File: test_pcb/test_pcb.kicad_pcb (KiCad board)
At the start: 2 copper layers, 2 parts

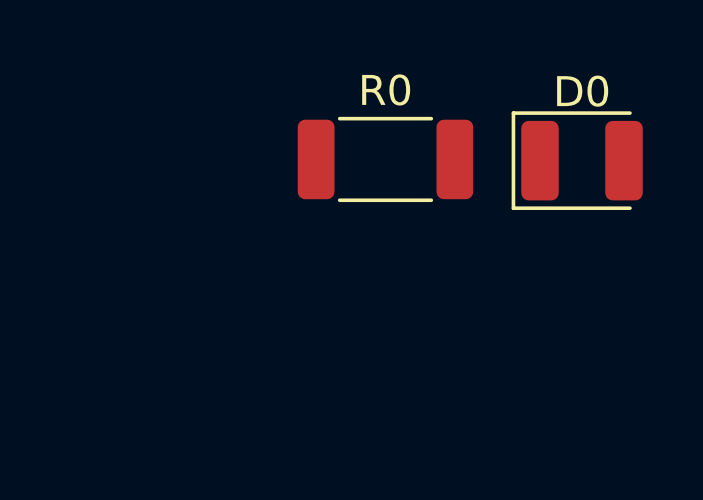
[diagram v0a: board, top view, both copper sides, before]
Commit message: added loading for segments and vias
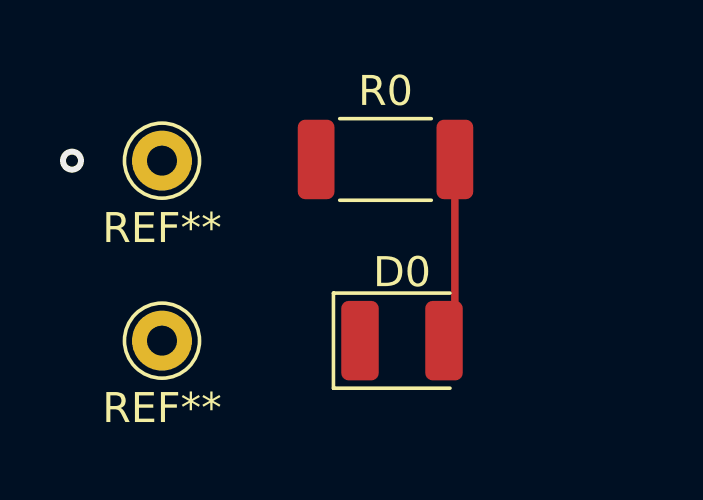
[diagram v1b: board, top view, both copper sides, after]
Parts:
- added REF**: Pin_D1.0mm_L10.0mm, Connector_Pin:Pin_D1.0mm_L10.0mm, F.Cu at (28.0, 39.0)
- added REF**: Pin_D1.0mm_L10.0mm, Connector_Pin:Pin_D1.0mm_L10.0mm, F.Cu at (28.0, 33.0)
- moved D0 8.49 mm to (36.0, 39.0)
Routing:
- net Net-(D0-Pad2): track 0.00 -> 6.19 mm
- net (no net): vias 0 -> 1
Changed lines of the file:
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@@
   (net 2 "Net-(D0-Pad2)")
   (net 3 "+5V")
+  (footprint "Connector_Pin:Pin_D1.0mm_L10.0mm" (layer "F.Cu")
+    (at 28 39)
+    (descr "solder Pin_ diameter 1.0mm, hole diameter 1.0mm (press fit), length 10.0mm")
+    (tags "solder Pin_ press fit")
+    (attr through_hole)
+    (fp_text reference "REF**" (at 0 2.25) (layer "F.SilkS")
+      (effects (font (size 1 1) (thickness 0.15)))
+    )
+    (fp_text value "Pin_D1.0mm_L10.0mm" (at 0 -2.05) (layer "F.Fab")
+      (effects (font (size 1 1) (thickness 0.15)))
+    )
+    (fp_text user "${REFERENCE}" (at 0 2.25) (layer "F.Fab")
+      (effects (font (size 1 1) (thickness 0.15)))
+    )
+    (fp_circle (center 0 0) (end 1.25 0.05) (layer "F.SilkS") (width 0.12) (fill none))
+    (fp_circle (center 0 0) (end 1.5 0) (layer "F.CrtYd") (width 0.05) (fill none))
+    (fp_circle (center 0 0) (end 0.5 0) (layer "F.Fab") (width 0.12) (fill none))
+    (fp_circle (center 0 0) (end 1 0) (layer "F.Fab") (width 0.12) (fill none))
+    (pad "1" thru_hole circle (at 0 0) (size 2 2) (drill 1) (layers *.Cu *.Mask)
+      (net 1 "GND"))
+    (model "${KICAD6_3DMODEL_DIR}/Connector_Pin.3dshapes/Pin_D1.0mm_L10.0mm.wrl"
+      (offset (xyz 0 0 0))
+      (scale (xyz 1 1 1))
+      (rotate (xyz 0 0 0))
+    )
+  )
   (footprint "LED_SMD:LED_1210_3225Metric" (layer "F.Cu")
-    (at 42 33)
+    (at 36 39)
     (descr "LED SMD 1210 (3225 Metric), square (rectangular) end terminal, IPC_7351 nominal, (Body size source: http://www.tortai-tech.com/upload/download/2011102023233369053.pdf), generated with kicad-footprint-generator")
     (tags "LED")
@@
       (net 2 "Net-(D0-Pad2)") (pinfunction "A") (pintype "passive"))
     (model "${KICAD6_3DMODEL_DIR}/LED_SMD.3dshapes/LED_1210_3225Metric.wrl"
+      (offset (xyz 0 0 0))
+      (scale (xyz 1 1 1))
+      (rotate (xyz 0 0 0))
+    )
+  )
+  (footprint "Connector_Pin:Pin_D1.0mm_L10.0mm" (layer "F.Cu")
+    (at 28 33)
+    (descr "solder Pin_ diameter 1.0mm, hole diameter 1.0mm (press fit), length 10.0mm")
+    (tags "solder Pin_ press fit")
+    (attr through_hole)
+    (fp_text reference "REF**" (at 0 2.25) (layer "F.SilkS")
+      (effects (font (size 1 1) (thickness 0.15)))
+    )
+    (fp_text value "Pin_D1.0mm_L10.0mm" (at 0 -2.05) (layer "F.Fab")
+      (effects (font (size 1 1) (thickness 0.15)))
+    )
+    (fp_text user "${REFERENCE}" (at 0 2.25) (layer "F.Fab")
+      (effects (font (size 1 1) (thickness 0.15)))
+    )
+    (fp_circle (center 0 0) (end 1.25 0.05) (layer "F.SilkS") (width 0.12) (fill none))
+    (fp_circle (center 0 0) (end 1.5 0) (layer "F.CrtYd") (width 0.05) (fill none))
+    (fp_circle (center 0 0) (end 0.5 0) (layer "F.Fab") (width 0.12) (fill none))
+    (fp_circle (center 0 0) (end 1 0) (layer "F.Fab") (width 0.12) (fill none))
+    (pad "1" thru_hole circle (at 0 0) (size 2 2) (drill 1) (layers *.Cu *.Mask)
+      (net 3 "+5V"))
+    (model "${KICAD6_3DMODEL_DIR}/Connector_Pin.3dshapes/Pin_D1.0mm_L10.0mm.wrl"
       (offset (xyz 0 0 0))
       (scale (xyz 1 1 1))
@@
     )
   )
+  (via (at 25 33) (size 0.8) (drill 0.4) (layers "F.Cu" "B.Cu") (free) (net 0))
+  (segment (start 37.7625 38.6375) (end 37.4 39) (width 0.25) (layer "F.Cu") (net 2))
+  (segment (start 37.7625 32.96) (end 37.7625 38.6375) (width 0.25) (layer "F.Cu") (net 2))
 )
